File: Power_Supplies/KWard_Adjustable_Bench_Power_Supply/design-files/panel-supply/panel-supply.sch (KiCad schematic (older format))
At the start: 13 parts

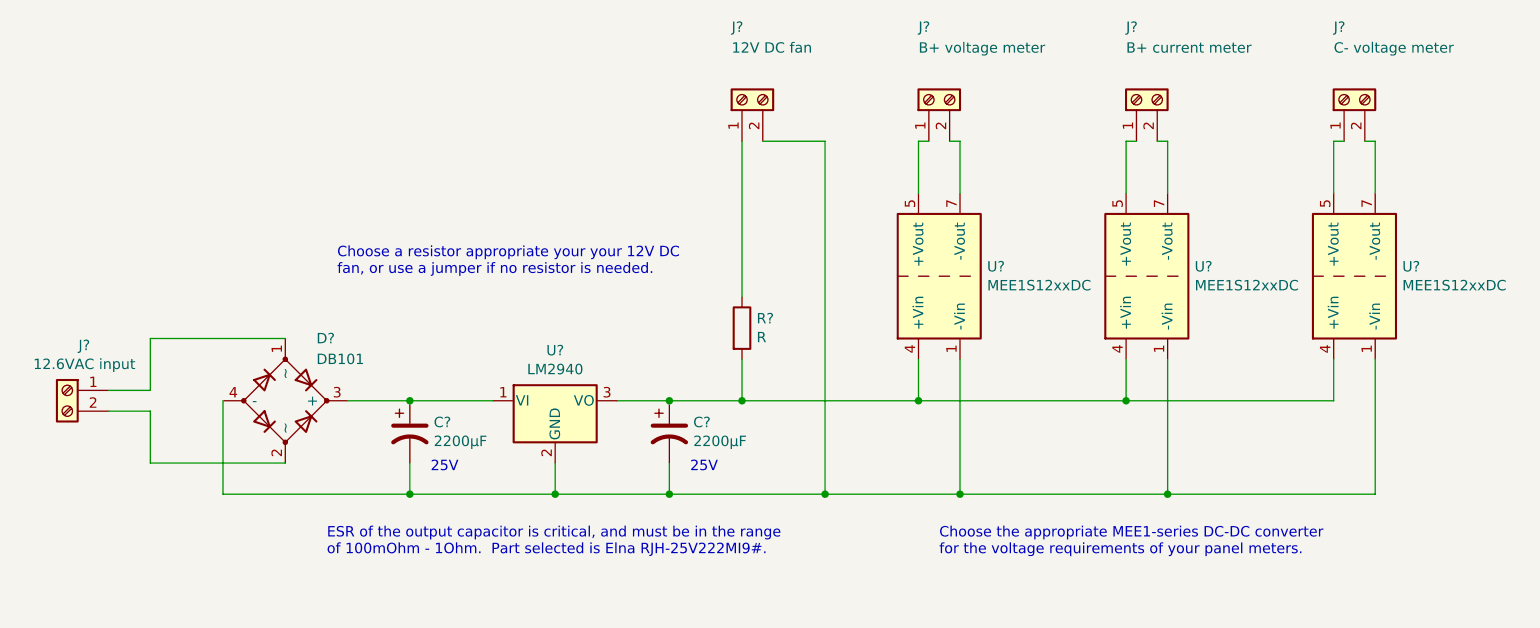
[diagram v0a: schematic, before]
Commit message: panel-supply: Small schematic tweaks made while laying out the PCB.
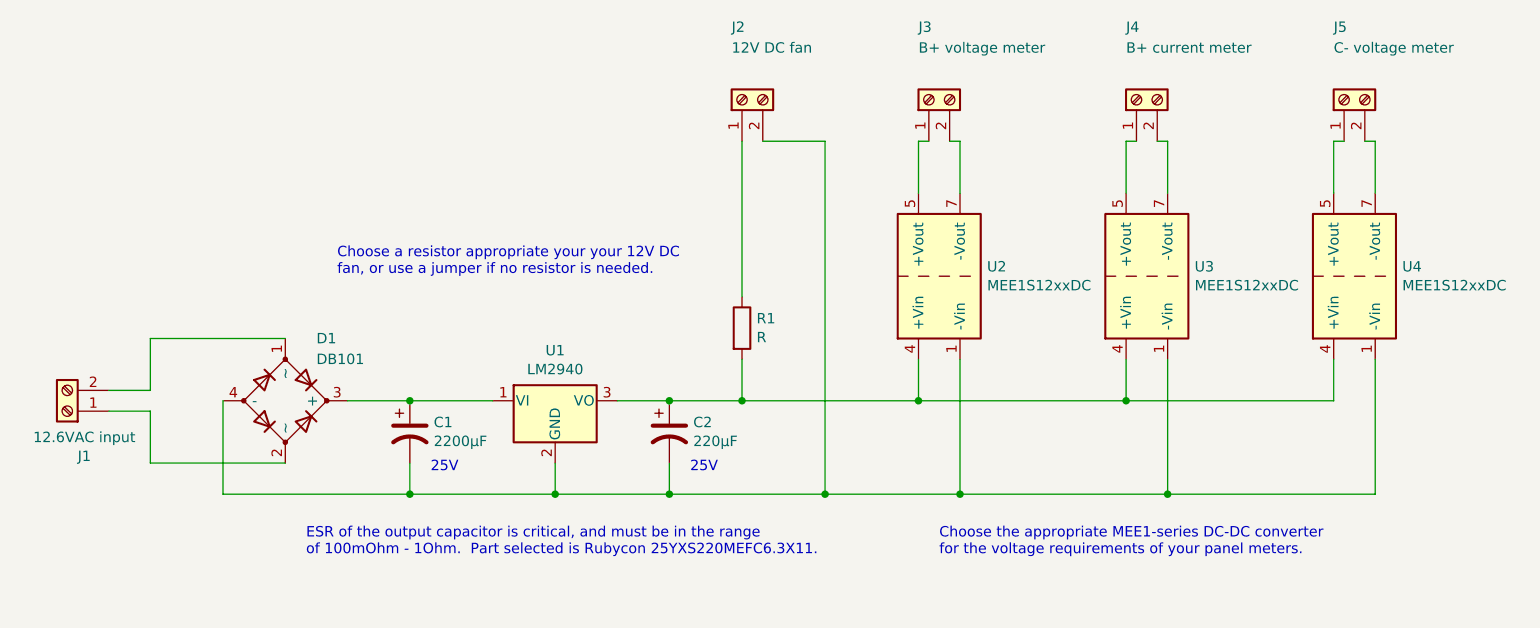
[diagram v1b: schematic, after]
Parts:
- C2: renamed from C?; value 2200µF -> 220µF; footprint Capacitor_THT:CP_Radial_D12.5mm_P5.00mm -> Capacitor_THT:CP_Radial_D6.3mm_P2.50mm; Mouser 555-RJH-25V222MI9# -> 25YXS220MEFC6.3X11
- D1: renamed from D?; footprint Package_DIP:DIP-4_W7.62mm -> Diodes_THT:Diode_Bridge_DIP-4_W7.62mm_P5.08mm
- R1: renamed from R?; footprint (none) -> Resistor_THT:R_Axial_DIN0309_L9.0mm_D3.2mm_P2.54mm_Vertical
- gave numbers to parts that had none: 10
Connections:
- net at J1.1 (Pin_1): now also D1.2 (~~); no longer D1.1 (~~)
- net at J1.2 (Pin_2): now also D1.1 (~~); no longer D1.2 (~~)
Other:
- note added: "ESR of the output capacitor is critical, and must be in the range\nof 100mOhm - 1Ohm. Part selected is Rubycon 25YXS220MEFC6.3X11."
- note removed: "ESR of the output capacitor is critical, and must be in the range\nof 100mOhm - 1Ohm. Part selected is Elna RJH-25V222MI9#."
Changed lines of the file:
@@
 $EndDescr
 $Comp
-L Connector:Screw_Terminal_01x02 J?
+L Connector:Screw_Terminal_01x02 J1
 U 1 1 641B17A4
-P 1750 4400
-F 0 "J?" H 1668 4617 50  0000 C CNN
-F 1 "12.6VAC input" H 1668 4526 50  0000 C CNN
-F 2 "TerminalBlock_TE-Connectivity:TerminalBlock_TE_282834-2_1x02_P2.54mm_Horizontal" H 1750 4400 50  0001 C CNN
-F 3 "~" H 1750 4400 50  0001 C CNN
-	1    1750 4400
-	-1   0    0    -1
-$EndComp
-$Comp
-L jrt-ICs:DB10x D?
+P 1750 4500
+F 0 "J1" H 1668 4717 50  0000 C CNN
+F 1 "12.6VAC input" H 1668 4626 50  0000 C CNN
+F 2 "TerminalBlock_TE-Connectivity:TerminalBlock_TE_282834-2_1x02_P2.54mm_Horizontal" H 1750 4500 50  0001 C CNN
+F 3 "~" H 1750 4500 50  0001 C CNN
+	1    1750 4500
+	-1   0    0    1
+$EndComp
+$Comp
+L jrt-ICs:DB10x D1
 U 1 1 641C3084
 P 2800 4450
-F 0 "D?" H 2950 4750 50  0000 L CNN
+F 0 "D1" H 2950 4750 50  0000 L CNN
 F 1 "DB101" H 2950 4650 50  0000 L CNN
-F 2 "Package_DIP:DIP-4_W7.62mm" H 2800 4450 50  0001 C CNN
+F 2 "Diodes_THT:Diode_Bridge_DIP-4_W7.62mm_P5.08mm" H 2800 4450 50  0001 C CNN
 F 3 "https://www.mouser.com/datasheet/2/345/db101s-1012s-17410.pdf" H 2800 4450 50  0001 C CNN
 	1    2800 4450
@@
 	2150 4750 2800 4750
 $Comp
-L Device:CP1 C?
+L Device:CP1 C1
 U 1 1 641C5CA9
 P 3400 4600
-F 0 "C?" H 3515 4646 50  0000 L CNN
+F 0 "C1" H 3515 4646 50  0000 L CNN
 F 1 "2200µF" H 3515 4555 50  0000 L CNN
 F 2 "Capacitor_THT:CP_Radial_D12.5mm_P5.00mm" H 3400 4600 50  0001 C CNN
@@
 25V
 $Comp
-L Regulator_Linear:LM2937xT U?
+L Regulator_Linear:LM2937xT U1
 U 1 1 641C7498
 P 4100 4450
-F 0 "U?" H 4100 4692 50  0000 C CNN
+F 0 "U1" H 4100 4692 50  0000 C CNN
 F 1 "LM2940" H 4100 4601 50  0000 C CNN
 F 2 "Package_TO_SOT_THT:TO-220-3_Vertical" H 4100 4675 50  0001 C CIN
@@
 Connection ~ 3400 4900
 $Comp
-L Device:CP1 C?
+L Device:CP1 C2
 U 1 1 641C9B64
 P 4650 4600
-F 0 "C?" H 4765 4646 50  0000 L CNN
-F 1 "2200µF" H 4765 4555 50  0000 L CNN
-F 2 "Capacitor_THT:CP_Radial_D12.5mm_P5.00mm" H 4650 4600 50  0001 C CNN
-F 3 "https://www.mouser.com/datasheet/2/129/RJH-4600.pdf" H 4650 4600 50  0001 C CNN
-F 4 "555-RJH-25V222MI9#" H 4650 4600 50  0001 C CNN "Mouser"
+F 0 "C2" H 4765 4646 50  0000 L CNN
+F 1 "220µF" H 4765 4555 50  0000 L CNN
+F 2 "Capacitor_THT:CP_Radial_D6.3mm_P2.50mm" H 4650 4600 50  0001 C CNN
+F 3 "https://www.mouser.com/datasheet/2/977/e_YXS-1600637.pdf" H 4650 4600 50  0001 C CNN
+F 4 "25YXS220MEFC6.3X11" H 4650 4600 50  0001 C CNN "Mouser"
 	1    4650 4600
 	1    0    0    -1
@@
 	4400 4450 4650 4450
 $Comp
-L jrt-ICs:MEE1SxxxxDC U?
+L jrt-ICs:MEE1SxxxxDC U2
 U 1 1 641DF49E
 P 5950 3850
-F 0 "U?" V 5996 3620 50  0000 R CNN
+F 0 "U2" V 5996 3620 50  0000 R CNN
 F 1 "MEE1S12xxDC" V 5905 3620 50  0000 R CNN
 F 2 "Package_DIP:DIP-8_W7.62mm" H 5950 3850 50  0001 C CNN
@@
 $EndComp
 $Comp
-L jrt-ICs:MEE1SxxxxDC U?
+L jrt-ICs:MEE1SxxxxDC U3
 U 1 1 641E07F9
 P 6950 3850
-F 0 "U?" V 6996 3620 50  0000 R CNN
+F 0 "U3" V 6996 3620 50  0000 R CNN
 F 1 "MEE1S12xxDC" V 6905 3620 50  0000 R CNN
 F 2 "Package_DIP:DIP-8_W7.62mm" H 6950 3850 50  0001 C CNN
@@
 $EndComp
 $Comp
-L jrt-ICs:MEE1SxxxxDC U?
+L jrt-ICs:MEE1SxxxxDC U4
 U 1 1 641E0D9C
 P 7950 3850
-F 0 "U?" V 7996 3620 50  0000 R CNN
+F 0 "U4" V 7996 3620 50  0000 R CNN
 F 1 "MEE1S12xxDC" V 7905 3620 50  0000 R CNN
 F 2 "Package_DIP:DIP-8_W7.62mm" H 7950 3850 50  0001 C CNN
@@
 $EndComp
 $Comp
-L Connector:Screw_Terminal_01x02 J?
+L Connector:Screw_Terminal_01x02 J2
 U 1 1 641E4A71
 P 5000 3000
-F 0 "J?" V 5350 3050 50  0000 R CNN
+F 0 "J2" V 5350 3050 50  0000 R CNN
 F 1 "12V DC fan" V 5250 3050 50  0000 R CNN
 F 2 "TerminalBlock_TE-Connectivity:TerminalBlock_TE_282834-2_1x02_P2.54mm_Horizontal" H 5000 3000 50  0001 C CNN
@@
 $EndComp
 $Comp
-L Device:R R?
+L Device:R R1
 U 1 1 641E5FA1
 P 5000 4100
-F 0 "R?" H 5070 4146 50  0000 L CNN
+F 0 "R1" H 5070 4146 50  0000 L CNN
 F 1 "R" H 5070 4055 50  0000 L CNN
-F 2 "" V 4930 4100 50  0001 C CNN
+F 2 "Resistor_THT:R_Axial_DIN0309_L9.0mm_D3.2mm_P2.54mm_Vertical" V 4930 4100 50  0001 C CNN
 F 3 "~" H 5000 4100 50  0001 C CNN
 	1    5000 4100
@@
 	7050 4900 8050 4900
 $Comp
-L Connector:Screw_Terminal_01x02 J?
+L Connector:Screw_Terminal_01x02 J3
 U 1 1 641E942C
 P 5900 3000
-F 0 "J?" V 6250 3050 50  0000 R CNN
+F 0 "J3" V 6250 3050 50  0000 R CNN
 F 1 "B+ voltage meter" V 6150 3050 50  0000 R CNN
 F 2 "TerminalBlock_TE-Connectivity:TerminalBlock_TE_282834-2_1x02_P2.54mm_Horizontal" H 5900 3000 50  0001 C CNN
@@
 $EndComp
 $Comp
-L Connector:Screw_Terminal_01x02 J?
+L Connector:Screw_Terminal_01x02 J4
 U 1 1 641E97BD
 P 6900 3000
-F 0 "J?" V 7250 3050 50  0000 R CNN
+F 0 "J4" V 7250 3050 50  0000 R CNN
 F 1 "B+ current meter" V 7150 3050 50  0000 R CNN
 F 2 "TerminalBlock_TE-Connectivity:TerminalBlock_TE_282834-2_1x02_P2.54mm_Horizontal" H 6900 3000 50  0001 C CNN
@@
 $EndComp
 $Comp
-L Connector:Screw_Terminal_01x02 J?
+L Connector:Screw_Terminal_01x02 J5
 U 1 1 641E9B02
 P 7900 3000
-F 0 "J?" V 8250 3050 50  0000 R CNN
+F 0 "J5" V 8250 3050 50  0000 R CNN
 F 1 "C- voltage meter" V 8150 3050 50  0000 R CNN
 F 2 "TerminalBlock_TE-Connectivity:TerminalBlock_TE_282834-2_1x02_P2.54mm_Horizontal" H 7900 3000 50  0001 C CNN
@@
 Text Notes 3050 3850 0    50   ~ 0
 Choose a resistor appropriate your your 12V DC\nfan, or use a jumper if no resistor is needed.
-Text Notes 3000 5200 0    50   ~ 0
-ESR of the output capacitor is critical, and must be in the range\nof 100mOhm - 1Ohm.  Part selected is Elna RJH-25V222MI9#.
+Text Notes 2900 5200 0    50   ~ 0
+ESR of the output capacitor is critical, and must be in the range\nof 100mOhm - 1Ohm.  Part selected is Rubycon 25YXS220MEFC6.3X11.
 $EndSCHEMATC

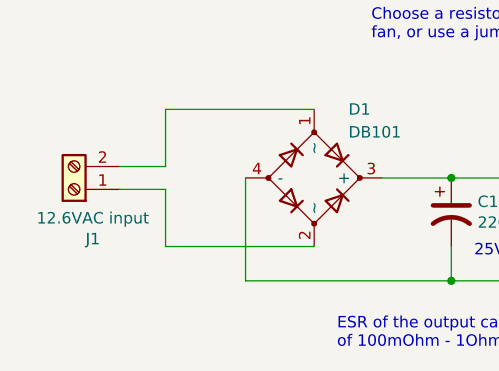
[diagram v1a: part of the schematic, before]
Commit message: panel-supply: Add a note specifying Triad F5-12 for the transformer.
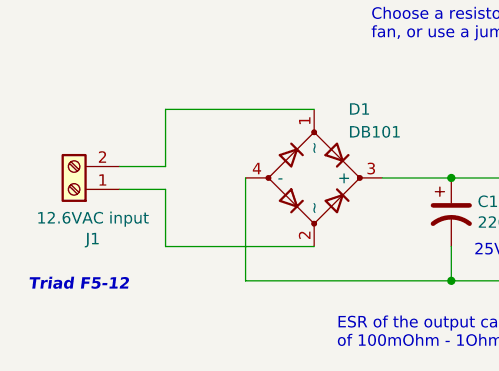
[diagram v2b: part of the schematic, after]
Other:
- note added: "Triad F5-12"
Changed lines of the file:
@@
 Text Notes 2900 5200 0    50   ~ 0
 ESR of the output capacitor is critical, and must be in the range\nof 100mOhm - 1Ohm.  Part selected is Rubycon 25YXS220MEFC6.3X11.
+Text Notes 1550 4950 0    50   Italic 10
+Triad F5-12
 $EndSCHEMATC

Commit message: Improve text comments.
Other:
- note added: "Choose a resistor appropriate your your 12Vdc\nfan if you wish to limit the current or drop some\nof the voltage, or use a jumper if no resistor is\nneeded."
- note added: "Choose the appropriate MEE1-series DC-DC converter\nfor the voltage requirements of your panel meters. If any\nof your meters are capable of runing at 12Vdc, then simply\ninstall jumpers between the appropriate pins of DC-DC\nconverter footprint(s)."
- note removed: "Choose a resistor appropriate your your 12V DC\nfan, or use a jumper if no resistor is needed."
- note removed: "Choose the appropriate MEE1-series DC-DC converter\nfor the voltage requirements of your panel meters."
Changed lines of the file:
@@
 Wire Wire Line
 	8050 3200 8050 3450
-Text Notes 5950 5200 0    50   ~ 0
-Choose the appropriate MEE1-series DC-DC converter\nfor the voltage requirements of your panel meters.
-Text Notes 3050 3850 0    50   ~ 0
-Choose a resistor appropriate your your 12V DC\nfan, or use a jumper if no resistor is needed.
+Text Notes 5950 5450 0    50   ~ 0
+Choose the appropriate MEE1-series DC-DC converter\nfor the voltage requirements of your panel meters.  If any\nof your meters are capable of runing at 12Vdc, then simply\ninstall jumpers between the appropriate pins of DC-DC\nconverter footprint(s).
+Text Notes 3050 3950 0    50   ~ 0
+Choose a resistor appropriate your your 12Vdc\nfan if you wish to limit the current or drop some\nof the voltage, or use a jumper if no resistor is\nneeded.
 Text Notes 2900 5200 0    50   ~ 0
 ESR of the output capacitor is critical, and must be in the range\nof 100mOhm - 1Ohm.  Part selected is Rubycon 25YXS220MEFC6.3X11.

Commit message: panel-supply: Final tweaks for 1.0.  Generate Gerber files.
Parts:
- C2: Mouser 25YXS220MEFC6.3X11 -> 232-25YXS220MEFC63X1
- D1: Mouser (none) -> 583-DB101
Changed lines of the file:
@@
 Sheet 1 1
 Title "KWard Bench PSU - Panel meter supply"
-Date ""
-Rev "0.1"
-Comp "Copyright (c) 2021 Jason R. Thorpe. See LICENSE."
+Date "2022-01-01"
+Rev "1.0"
+Comp "Copyright (c) 2017-2022 Kevin Ward and Jason R. Thorpe. See LICENSE."
 Comment1 ""
 Comment2 ""
@@
 F 2 "Diodes_THT:Diode_Bridge_DIP-4_W7.62mm_P5.08mm" H 2800 4450 50  0001 C CNN
 F 3 "https://www.mouser.com/datasheet/2/345/db101s-1012s-17410.pdf" H 2800 4450 50  0001 C CNN
+F 4 "583-DB101" H 2800 4450 50  0001 C CNN "Mouser"
 	1    2800 4450
 	1    0    0    -1
@@
 F 2 "Capacitor_THT:CP_Radial_D6.3mm_P2.50mm" H 4650 4600 50  0001 C CNN
 F 3 "https://www.mouser.com/datasheet/2/977/e_YXS-1600637.pdf" H 4650 4600 50  0001 C CNN
-F 4 "25YXS220MEFC6.3X11" H 4650 4600 50  0001 C CNN "Mouser"
+F 4 "232-25YXS220MEFC63X1" H 4650 4600 50  0001 C CNN "Mouser"
 	1    4650 4600
 	1    0    0    -1
